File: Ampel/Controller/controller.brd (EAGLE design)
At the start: 48.2 x 35 mm, 15 parts, among them IC1 ATtiny25, IC2 7805TV, X1 22-23-2041, X2 KUSBVX

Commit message: Stecker angepasst
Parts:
- removed X1: 22-23-2041, con-molex:22-23-2041
- added U$1: (no value), n39:PSW_5
- moved SV1 1.27 mm to (38.1, 19.1)
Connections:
- net GND: now also U$1.GND1, U$1.GND2; no longer X1.2, X1.3
- net VCC: now also U$1.-5V; no longer X1.4
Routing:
- net VCC: track 154.0 -> 160.4 mm
- net SCK: track 40.6 -> 41.9 mm
- net RESET: track 43.2 -> 44.5 mm
- net MOSI: track 19.1 -> 20.3 mm
- net MISO: track 29.2 -> 30.5 mm
- net GND: track 112.8 -> 112.2 mm
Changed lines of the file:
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@@
 <element name="R1" library="resistor" package="0207/10" value="10K" x="20.32" y="12.7" rot="R270"/>
 <element name="C1" library="resistor" package="C025-024X044" value="10n" x="20.32" y="21.59" rot="R270"/>
-<element name="SV1" library="con-lstb" package="MA03-2" value="ISP" x="36.83" y="19.05">
-<attribute name="OC_NEWARK" value="unknown" x="55.88" y="1.27" size="1.778" layer="27" display="off"/>
-<attribute name="MPN" value="" x="55.88" y="1.27" size="1.778" layer="27" display="off"/>
-<attribute name="MF" value="" x="55.88" y="1.27" size="1.778" layer="27" display="off"/>
-<attribute name="OC_FARNELL" value="unknown" x="55.88" y="1.27" size="1.778" layer="27" display="off"/>
-</element>
-<element name="X1" library="con-molex" package="22-23-2041" value="22-23-2041" x="40.64" y="29.21">
-<attribute name="OC_NEWARK" value="38C0355" x="40.64" y="29.21" size="1.778" layer="27" display="off"/>
-<attribute name="MPN" value="22-23-2041" x="40.64" y="29.21" size="1.778" layer="27" display="off"/>
-<attribute name="MF" value="MOLEX" x="40.64" y="29.21" size="1.778" layer="27" display="off"/>
-<attribute name="OC_FARNELL" value="1462920" x="40.64" y="29.21" size="1.778" layer="27" display="off"/>
+<element name="SV1" library="con-lstb" package="MA03-2" value="ISP" x="38.1" y="19.05">
+<attribute name="OC_NEWARK" value="unknown" x="57.15" y="1.27" size="1.778" layer="27" display="off"/>
+<attribute name="MPN" value="" x="57.15" y="1.27" size="1.778" layer="27" display="off"/>
+<attribute name="MF" value="" x="57.15" y="1.27" size="1.778" layer="27" display="off"/>
+<attribute name="OC_FARNELL" value="unknown" x="57.15" y="1.27" size="1.778" layer="27" display="off"/>
 </element>
 <element name="OUT1" library="con-lstb" package="MA03-1" value="RED" x="30.48" y="29.21" rot="R90">
@@
 <element name="IC2" library="linear" package="TO220V" value="7805TV" x="5.46" y="30.19" rot="R90"/>
 <element name="JP1" library="pinhead" package="1X02" value="" x="5.08" y="21.59" rot="R270"/>
+<element name="U$1" library="n39" package="PSW_5" value="" x="49.53" y="22.86" rot="R270"/>
 </elements>
 <signals>
@@
 <contactref element="C1" pad="1"/>
 <contactref element="SV1" pad="2"/>
-<contactref element="X1" pad="4"/>
 <wire x1="20.32" y1="22.86" x2="22.86" y2="22.86" width="0.4064" layer="16"/>
 <wire x1="22.86" y1="22.86" x2="22.86" y2="21.59" width="0.4064" layer="16"/>
@@
 <wire x1="21.59" y1="3.81" x2="35.56" y2="3.81" width="0.4064" layer="16"/>
 <wire x1="35.56" y1="3.81" x2="35.56" y2="12.7" width="0.4064" layer="16"/>
-<wire x1="35.56" y1="12.7" x2="40.64" y2="12.7" width="0.4064" layer="16"/>
-<wire x1="40.64" y1="12.7" x2="40.64" y2="19.05" width="0.4064" layer="16"/>
-<wire x1="40.64" y1="19.05" x2="44.45" y2="19.05" width="0.4064" layer="16"/>
-<wire x1="44.45" y1="19.05" x2="44.45" y2="29.21" width="0.4064" layer="16"/>
-<wire x1="44.45" y1="31.75" x2="44.45" y2="29.21" width="0.8128" layer="16"/>
+<wire x1="35.56" y1="12.7" x2="41.91" y2="12.7" width="0.4064" layer="16"/>
+<wire x1="41.91" y1="12.7" x2="41.91" y2="15.24" width="0.4064" layer="16"/>
+<wire x1="41.91" y1="15.24" x2="41.91" y2="19.05" width="0.4064" layer="16"/>
 <wire x1="20.32" y1="17.78" x2="22.86" y2="17.78" width="0.4064" layer="16"/>
 <wire x1="22.86" y1="17.78" x2="22.86" y2="21.59" width="0.4064" layer="16"/>
@@
 <contactref element="OUT2" pad="3"/>
 <wire x1="30.48" y1="31.75" x2="21.59" y2="31.75" width="0.8128" layer="16"/>
-<wire x1="30.48" y1="31.75" x2="44.45" y2="31.75" width="0.8128" layer="16"/>
-<wire x1="34.29" y1="20.32" x2="34.29" y2="19.05" width="0.4064" layer="16"/>
+<wire x1="35.56" y1="20.32" x2="35.56" y2="19.05" width="0.4064" layer="16"/>
 <contactref element="D2" pad="C"/>
 <contactref element="C2" pad="1"/>
@@
 <wire x1="11.43" y1="31.75" x2="11.43" y2="29.21" width="0.8128" layer="16"/>
 <wire x1="21.59" y1="31.75" x2="11.43" y2="31.75" width="0.8128" layer="16"/>
-<wire x1="34.29" y1="19.05" x2="40.64" y2="19.05" width="0.4064" layer="16"/>
+<wire x1="35.56" y1="19.05" x2="41.91" y2="19.05" width="0.4064" layer="16"/>
+<contactref element="U$1" pad="-5V"/>
+<wire x1="43.43" y1="15.24" x2="41.91" y2="15.24" width="0.4064" layer="16"/>
+<wire x1="30.48" y1="31.75" x2="39.37" y2="31.75" width="0.8128" layer="16"/>
+<wire x1="39.37" y1="31.75" x2="39.37" y2="27.94" width="0.8128" layer="16"/>
+<wire x1="39.37" y1="27.94" x2="45.72" y2="27.94" width="0.8128" layer="16"/>
+<wire x1="45.72" y1="27.94" x2="45.72" y2="15.24" width="0.8128" layer="16"/>
+<wire x1="45.72" y1="15.24" x2="43.43" y2="15.24" width="0.8128" layer="16"/>
 </signal>
 <signal name="GND">
@@
 <contactref element="C1" pad="2"/>
 <contactref element="SV1" pad="6"/>
-<contactref element="X1" pad="3"/>
-<contactref element="X1" pad="2"/>
 <contactref element="OUT1" pad="1"/>
 <contactref element="OUT2" pad="1"/>
@@
 <wire x1="24.13" y1="30.48" x2="17.78" y2="30.48" width="0.4064" layer="16"/>
 <wire x1="17.78" y1="30.48" x2="17.78" y2="24.13" width="0.4064" layer="16"/>
-<wire x1="40.64" y1="24.13" x2="34.29" y2="24.13" width="0.4064" layer="16"/>
-<wire x1="34.29" y1="24.13" x2="34.29" y2="30.48" width="0.4064" layer="16"/>
-<wire x1="34.29" y1="30.48" x2="24.13" y2="30.48" width="0.4064" layer="16"/>
 <wire x1="24.13" y1="30.48" x2="24.13" y2="26.67" width="0.4064" layer="16"/>
 <contactref element="D2" pad="A"/>
@@
 <wire x1="17.78" y1="20.32" x2="16.2" y2="20.32" width="0.4064" layer="16"/>
 <wire x1="16.2" y1="20.32" x2="16.2" y2="7.62" width="0.4064" layer="16"/>
-<wire x1="39.37" y1="29.21" x2="41.91" y2="29.21" width="0.4064" layer="16"/>
-<wire x1="41.91" y1="29.21" x2="41.91" y2="25.4" width="0.4064" layer="16"/>
-<wire x1="41.91" y1="25.4" x2="40.64" y2="24.13" width="0.4064" layer="16"/>
 <contactref element="IC2" pad="2"/>
 <wire x1="13.97" y1="20.32" x2="16.2" y2="20.32" width="0.4064" layer="16"/>
 <contactref element="JP1" pad="1"/>
+<contactref element="U$1" pad="GND2"/>
+<contactref element="U$1" pad="GND1"/>
+<wire x1="40.64" y1="20.32" x2="35.56" y2="30.48" width="0.4064" layer="16"/>
+<wire x1="35.56" y1="30.48" x2="16.51" y2="30.48" width="0.4064" layer="16"/>
 </signal>
 <signal name="RESET">
@@
 <wire x1="22.86" y1="13.97" x2="20.32" y2="13.97" width="0.4064" layer="16"/>
 <wire x1="20.32" y1="13.97" x2="20.32" y2="7.62" width="0.4064" layer="16"/>
-<wire x1="39.37" y1="17.78" x2="39.37" y2="13.97" width="0.4064" layer="16"/>
-<wire x1="39.37" y1="13.97" x2="34.29" y2="13.97" width="0.4064" layer="16"/>
+<wire x1="40.64" y1="17.78" x2="40.64" y2="13.97" width="0.4064" layer="16"/>
+<wire x1="40.64" y1="13.97" x2="34.29" y2="13.97" width="0.4064" layer="16"/>
 <wire x1="34.29" y1="13.97" x2="34.29" y2="5.08" width="0.4064" layer="16"/>
 <wire x1="34.29" y1="5.08" x2="22.86" y2="5.08" width="0.4064" layer="16"/>
@@
 <wire x1="27.94" y1="25.4" x2="27.94" y2="21.59" width="0.4064" layer="16"/>
 <wire x1="27.94" y1="21.59" x2="27.94" y2="17.78" width="0.4064" layer="16"/>
-<wire x1="27.94" y1="17.78" x2="34.29" y2="17.78" width="0.4064" layer="16"/>
+<wire x1="27.94" y1="17.78" x2="35.56" y2="17.78" width="0.4064" layer="16"/>
 </signal>
 <signal name="SCK">
@@
 <wire x1="24.13" y1="10.16" x2="24.13" y2="21.59" width="0.4064" layer="16"/>
 <wire x1="24.13" y1="21.59" x2="25.4" y2="21.59" width="0.4064" layer="16"/>
-<wire x1="36.83" y1="17.78" x2="36.83" y2="15.24" width="0.4064" layer="16"/>
-<wire x1="36.83" y1="15.24" x2="33.02" y2="15.24" width="0.4064" layer="16"/>
+<wire x1="38.1" y1="17.78" x2="38.1" y2="15.24" width="0.4064" layer="16"/>
+<wire x1="38.1" y1="15.24" x2="33.02" y2="15.24" width="0.4064" layer="16"/>
 <wire x1="33.02" y1="15.24" x2="33.02" y2="6.35" width="0.4064" layer="16"/>
 <wire x1="33.02" y1="6.35" x2="24.13" y2="6.35" width="0.4064" layer="16"/>
@@
 <wire x1="30.48" y1="21.59" x2="30.48" y2="22.86" width="0.4064" layer="16"/>
 <wire x1="30.48" y1="22.86" x2="33.02" y2="22.86" width="0.4064" layer="16"/>
-<wire x1="33.02" y1="22.86" x2="36.83" y2="22.86" width="0.4064" layer="16"/>
-<wire x1="36.83" y1="22.86" x2="36.83" y2="20.32" width="0.4064" layer="16"/>
+<wire x1="33.02" y1="22.86" x2="38.1" y2="22.86" width="0.4064" layer="16"/>
+<wire x1="38.1" y1="22.86" x2="38.1" y2="20.32" width="0.4064" layer="16"/>
 </signal>
 <signal name="N$1">
@@
 </signal>
 </signals>
+<errors>
+</errors>
 </board>
 </drawing>

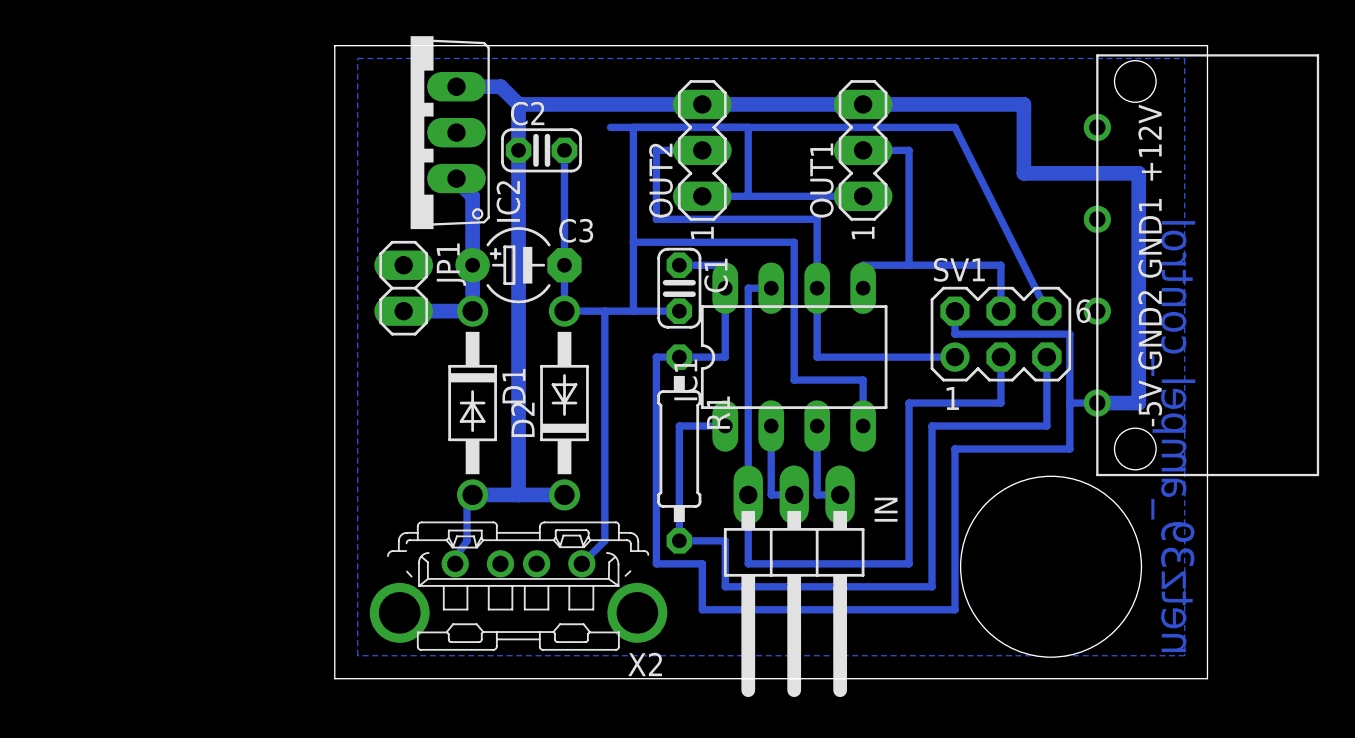
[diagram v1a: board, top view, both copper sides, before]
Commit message: Redesign des Controller-Boards auf I2C
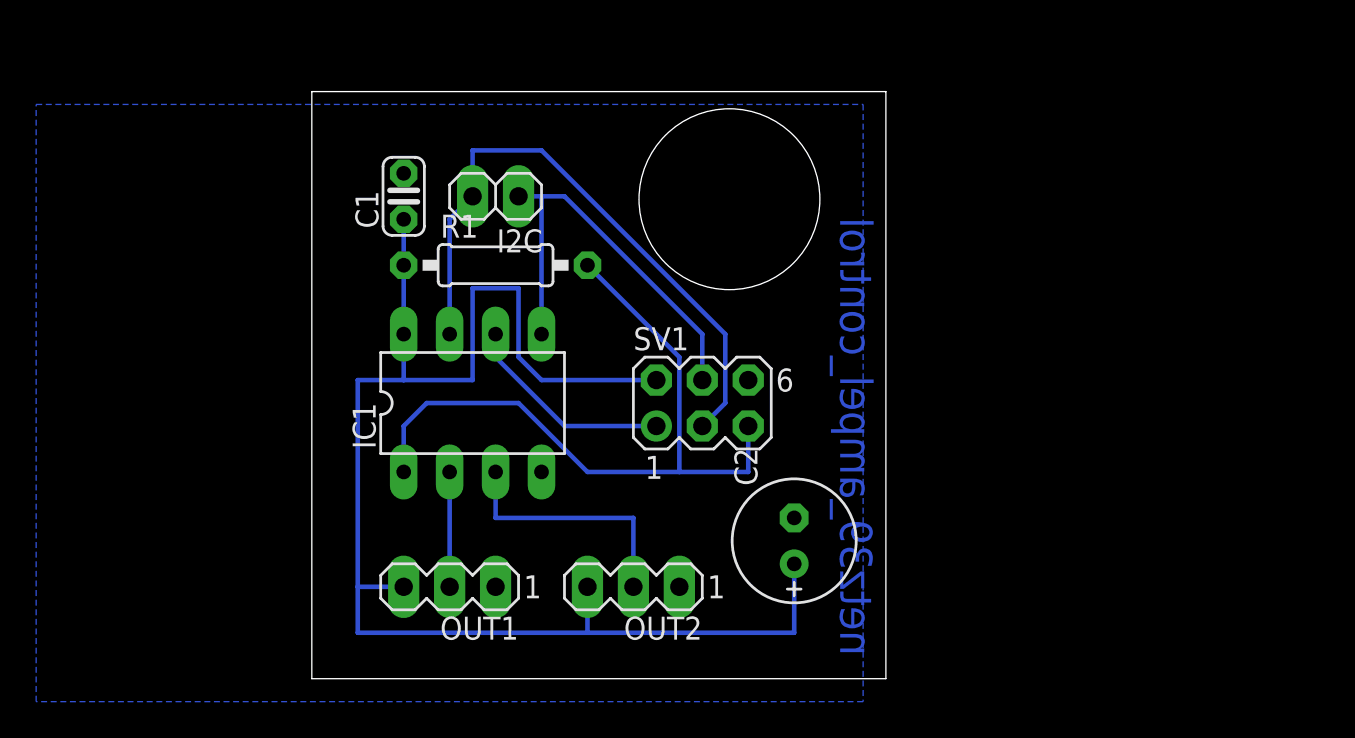
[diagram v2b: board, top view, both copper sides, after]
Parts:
- removed C3: 47µ, resistor:E5-4
- removed D1, D2: 1N4004, diode:DO41-10
- removed IC2: 7805TV, linear:TO220V
- removed IN: (no value), pinhead:1X03/90
- removed JP1: (no value), pinhead:1X02
- removed U$1: (no value), n39:PSW_5
- removed X2: KUSBVX, con-kycon:KUSBVX
- added I2C: (no value), pinhead:1X02
- C2: value 0.1µ -> 100u; device resistor:C025-024X044 -> resistor:E2,5-7
- moved OUT1 33.2 mm to (7.62, 5.08), turned to 180 degrees
- moved C2 25.7 mm to (26.7, 7.62), turned to 90 degrees
- moved OUT2 24.4 mm to (17.8, 5.08), turned to 180 degrees
- moved IC1 18.0 mm to (8.89, 15.2)
- moved SV1 16.9 mm to (21.6, 15.2)
- moved C1 16.1 mm to (5.08, 26.7), turned to 90 degrees
- moved R1 14.4 mm to (10.2, 22.9), turned to 0 degrees
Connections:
- removed net VEE: C3.+, D1.C, IC2.1, JP1.2
- net GND: now also C2.-; no longer C2.2, C3.-, D2.A, IC2.2, JP1.1, U$1.GND1, U$1.GND2, X2.4
- net MISO: no longer OUT2.2
- net MOSI: now also I2C.1; no longer OUT1.2
- net N$1: now also IC1.3, OUT2.2; no longer IC1.2, IN.2
- net N$2: now also IC1.2, OUT1.2; no longer IC1.3, IN.1
- net SCK: now also I2C.2; no longer IN.3
- net VCC: now also C2.+; no longer C2.1, D1.A, D2.C, IC2.3, U$1.-5V, X2.1
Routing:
- net GND: track 112.2 -> 0.00 mm
- net VCC: track 160.4 -> 81.8 mm
- net MISO: track 30.5 -> 11.7 mm
- net VEE: track 11.5 -> 0.00 mm
- net N$1: track 5.08 -> 14.0 mm
- net SCK: track 41.9 -> 34.5 mm
- net RESET: track 44.5 -> 39.8 mm
- net MOSI: track 20.3 -> 23.5 mm
- net N$2: track 5.08 -> 6.35 mm
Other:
- board size 48.2 x 35 mm -> 31.7 x 32.5 mm
